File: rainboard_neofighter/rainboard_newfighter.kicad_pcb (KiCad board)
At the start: 2 copper layers, 270.2 x 259 mm, 95 parts, among them J1 Conn_01x02, J10 Conn_01x03, J11 SDS-50J, J12 SDS-50J, J13 Conn_01x02, J14 Conn_01x02, J15 Conn_01x02, J16 Conn_01x02, J17 Conn_01x02, J18 Conn_01x02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

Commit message: use corrent JST-HX connector
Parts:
- J1, J13, J14, J15, J16, J17, J18, J2, J3, J4, J5, J6, J7, J8: footprint Connector_JST:JST_XH_S2B-XH-A-1_1x02_P2.50mm_Horizontal -> Connector_JST:JST_XH_B2B-XH-AM_1x02_P2.50mm_Vertical
- J10, J9: footprint Connector_JST:JST_XH_S3B-XH-A-1_1x03_P2.50mm_Horizontal -> Connector_JST:JST_XH_B3B-XH-A_1x03_P2.50mm_Vertical
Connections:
- XA1 pad D17: Net-(XA1-PadD17) -> button-38
- XA1 pad D18: button-28 -> MIDI-OUT
- XA1 pad D19: button-38 -> MIDI-IN
- XA1 pad D21: Net-(XA1-PadD21) -> button-28

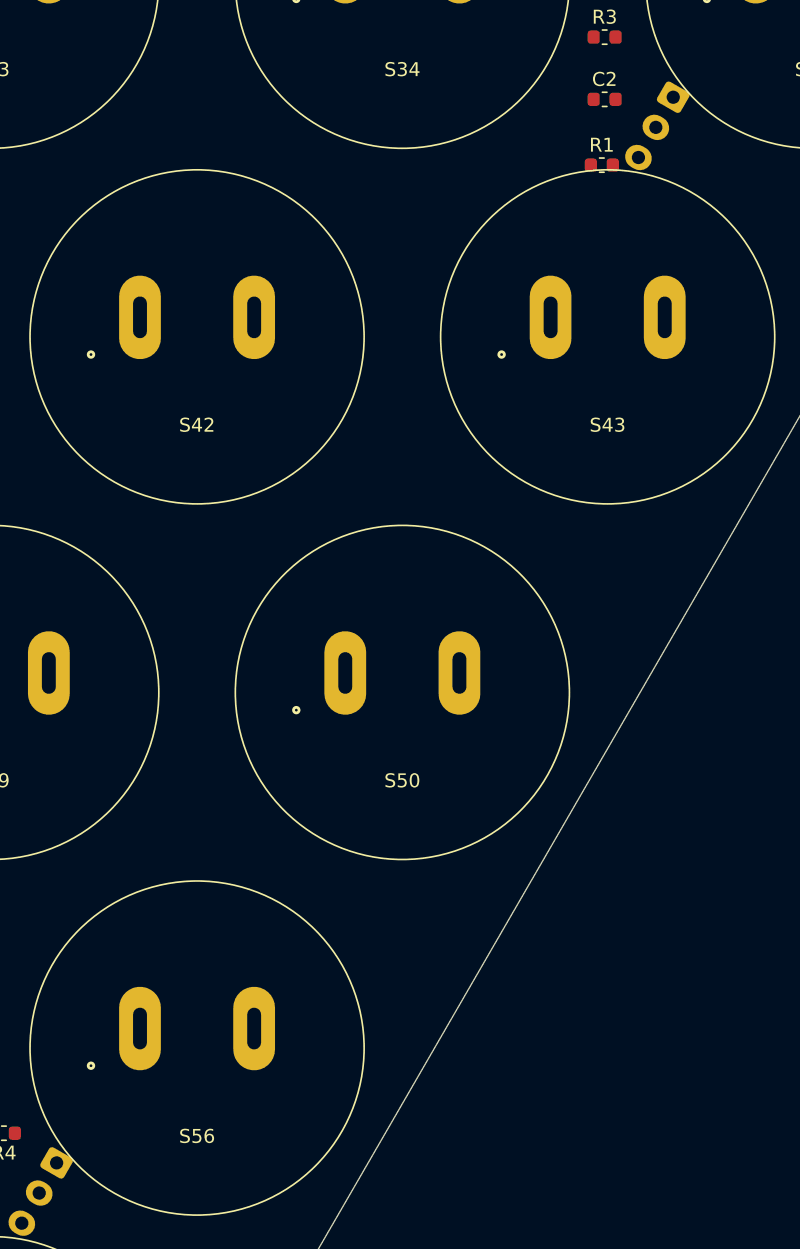
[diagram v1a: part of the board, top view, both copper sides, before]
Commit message: use corrent JST-HX connector
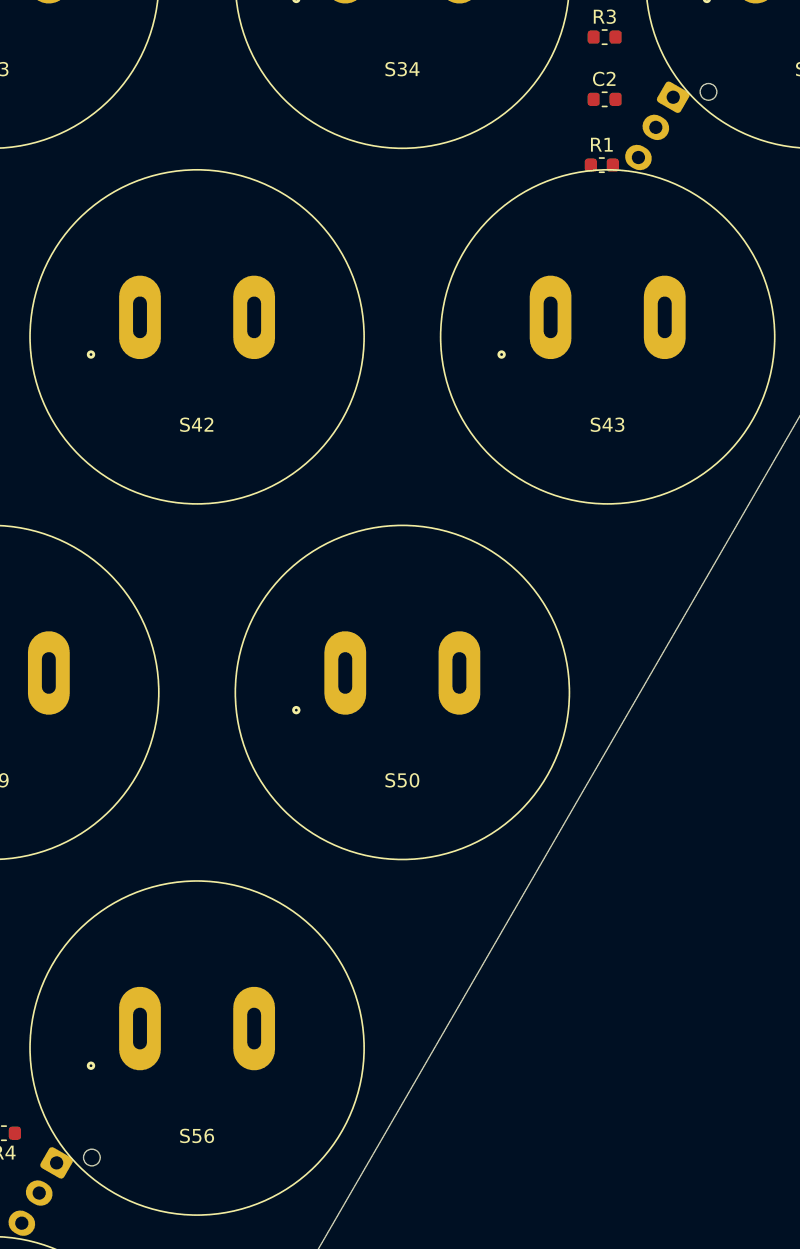
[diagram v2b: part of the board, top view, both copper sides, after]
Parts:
- J10, J9: footprint Connector_JST:JST_XH_B3B-XH-A_1x03_P2.50mm_Vertical -> Connector_JST:JST_XH_B3B-XH-AM_1x03_P2.50mm_Vertical

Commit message: final board outline dimentions
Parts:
- moved C1 39.1 mm to (0.41, -77.1)
- moved J11 8.70 mm to (-36.0, 128.2)
- moved J12 7.83 mm to (-15.3, 128.1)
- moved R1 6.67 mm to (96.2, 12.8)
- moved R4 3.75 mm to (59.3, 79.0)
- moved R5 3.28 mm to (-51.4, 119.5)
- moved C2 2.84 mm to (100.2, 8.99)
- moved C4 2.60 mm to (-56.2, 120.5)
- moved XA1 2.35 mm to (43.5, 137.5)
- moved R2 2.14 mm to (54.8, 86.6)
- moved R6 0.65 mm to (-43.7, 121.7)
- moved R3 0.37 mm to (102.7, 4.11)
- turned S39 to 0 degrees
- turned S41 to 0 degrees
- turned S59 to 270 degrees
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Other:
- board size 270.2 x 259 mm -> 260 x 253.6 mm

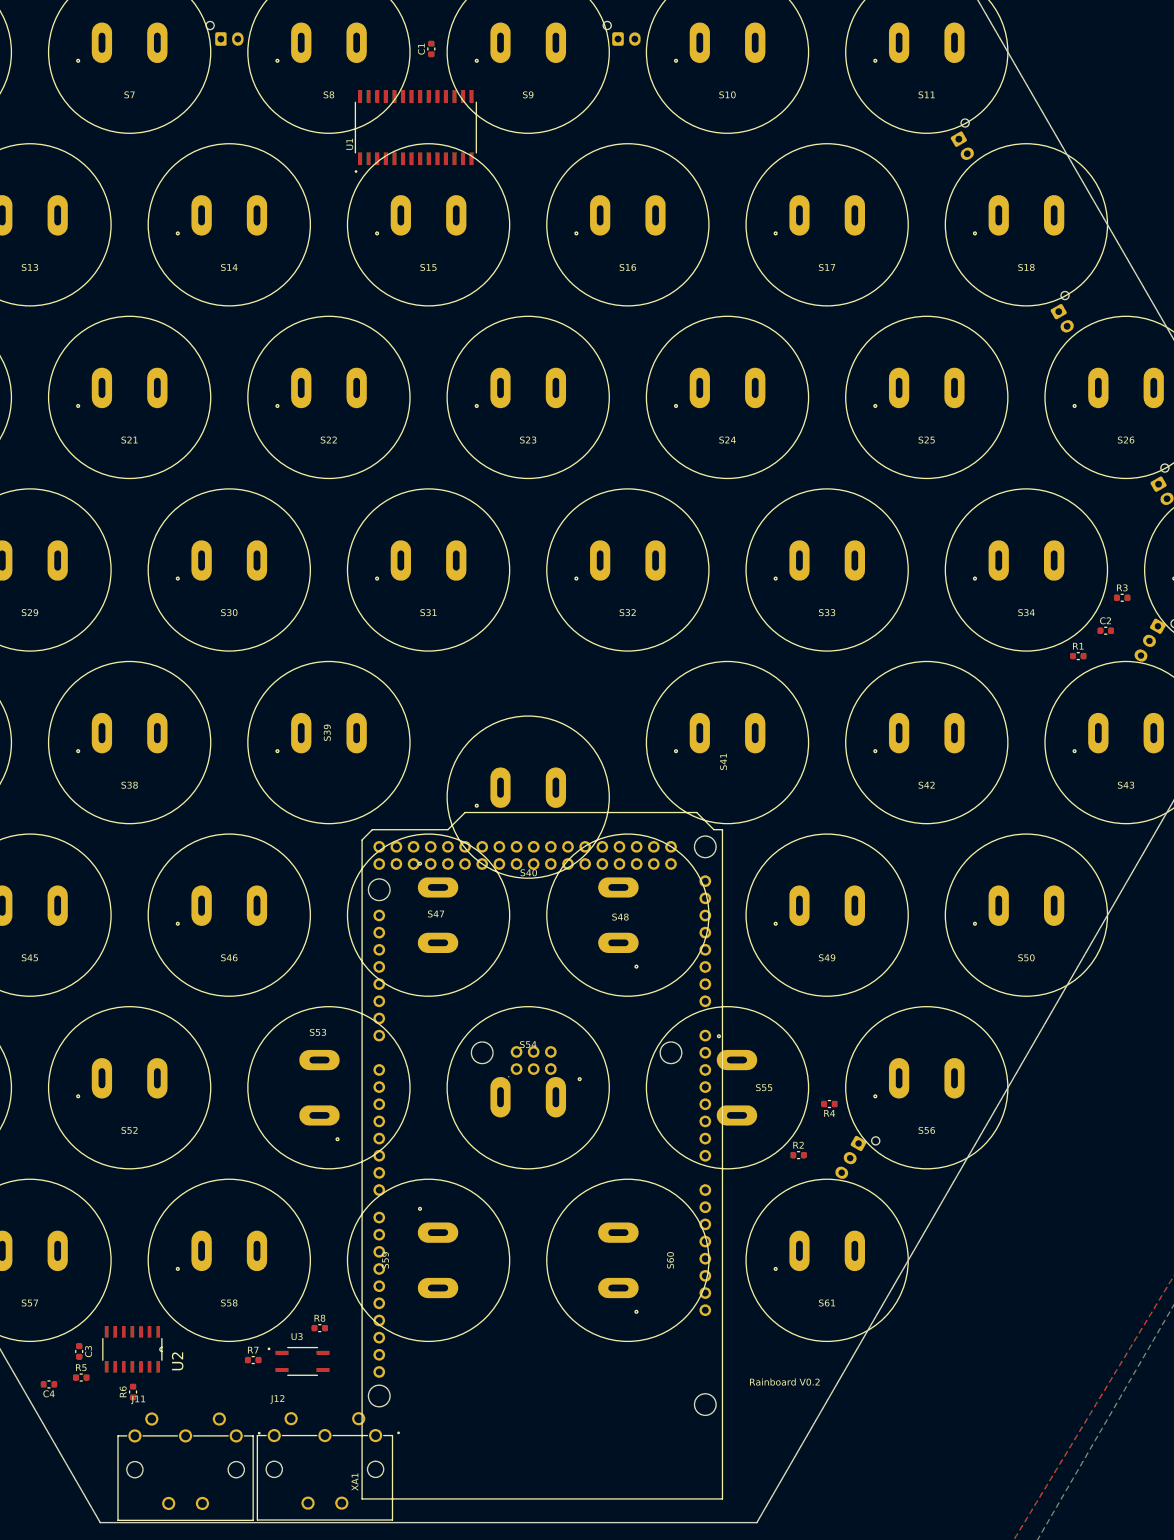
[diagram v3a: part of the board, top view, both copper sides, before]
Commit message: move decoupling caps close to ICs
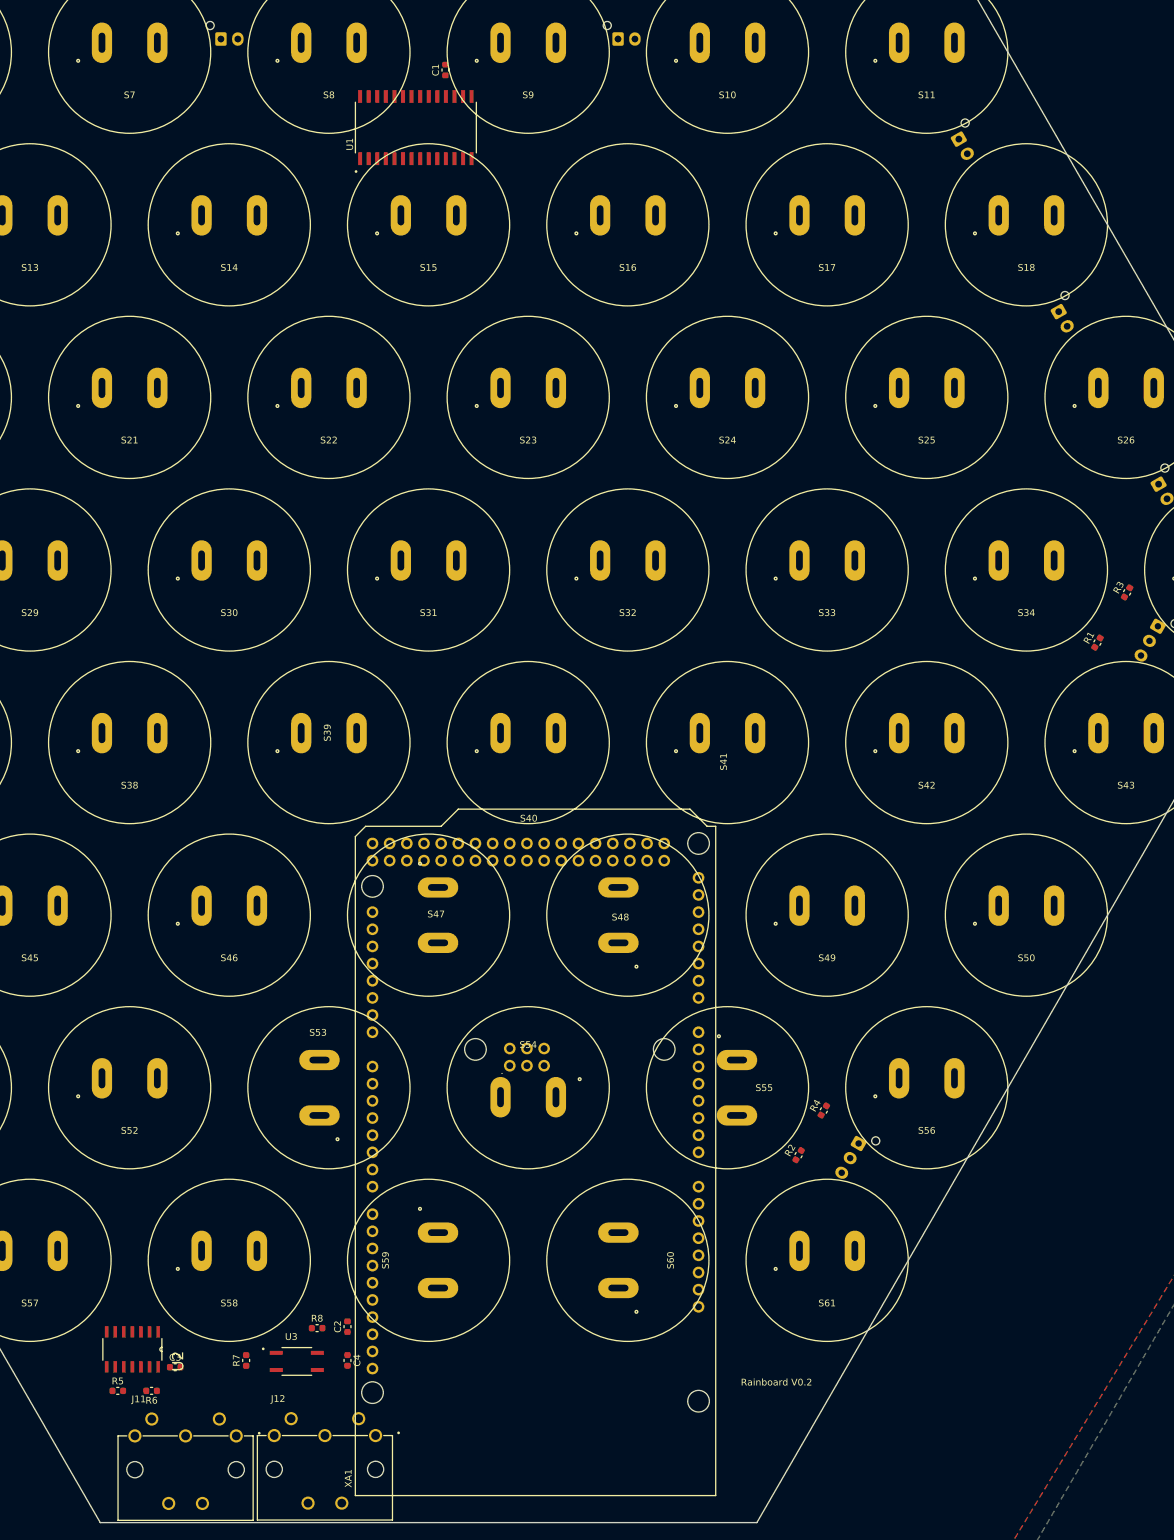
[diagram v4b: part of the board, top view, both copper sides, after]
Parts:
- moved C2 152.3 mm to (-12.0, 112.0), turned to 90 degrees
- moved C4 44.3 mm to (-12.0, 117.0), turned to 270 degrees
- moved C3 14.4 mm to (-37.5, 118.0), turned to 0 degrees
- moved S40 8.08 mm to (14.7, 25.5)
- moved R5 5.76 mm to (-46.0, 121.5)
- moved C1 3.75 mm to (2.50, -74.0)
- moved R1 3.47 mm to (99.0, 10.8), turned to 60 degrees
- moved R6 2.74 mm to (-41.0, 121.5), turned to 180 degrees
- moved R4 1.27 mm to (58.5, 80.0), turned to 60 degrees
- moved XA1 1.12 mm to (42.5, 137.0)
- moved R3 1.08 mm to (103.4, 3.32), turned to 60 degrees
- moved R7 1.04 mm to (-27.0, 117.0), turned to 90 degrees
- moved U3 0.86 mm to (-19.5, 117.1)
- moved R8 0.40 mm to (-16.5, 112.2)
- turned R2 to 60 degrees

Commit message: Add LCSC JLCPCB part data for each component
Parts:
- C1, C2, C3, C4: value 0.1uf -> 100nf
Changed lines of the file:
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@@
       (effects (font (size 1 1) (thickness 0.15)))
     )
-    (fp_text value 0.1uf (at 0 1.43 90) (layer F.Fab)
+    (fp_text value 100nf (at 0 1.43 90) (layer F.Fab)
       (effects (font (size 1 1) (thickness 0.15)))
     )
@@
       (effects (font (size 1 1) (thickness 0.15)))
     )
-    (fp_text value 0.1uf (at 0 1.43) (layer F.Fab)
+    (fp_text value 100nf (at 0 1.43) (layer F.Fab)
       (effects (font (size 1 1) (thickness 0.15)))
     )
@@
       (effects (font (size 1 1) (thickness 0.15)))
     )
-    (fp_text value 0.1uf (at 0 1.43 90) (layer F.Fab)
+    (fp_text value 100nf (at 0 1.43 90) (layer F.Fab)
       (effects (font (size 1 1) (thickness 0.15)))
     )
@@
       (effects (font (size 1 1) (thickness 0.15)))
     )
-    (fp_text value 0.1uf (at 0 1.43 90) (layer F.Fab)
-      (effects (font (size 1 1) (thickness 0.15)))
-    )
+    (fp_text value 100nf (at 0 1.43 90) (layer F.Fab)
+      (effects (font (size 1 1) (thickness 0.15)))
+    )

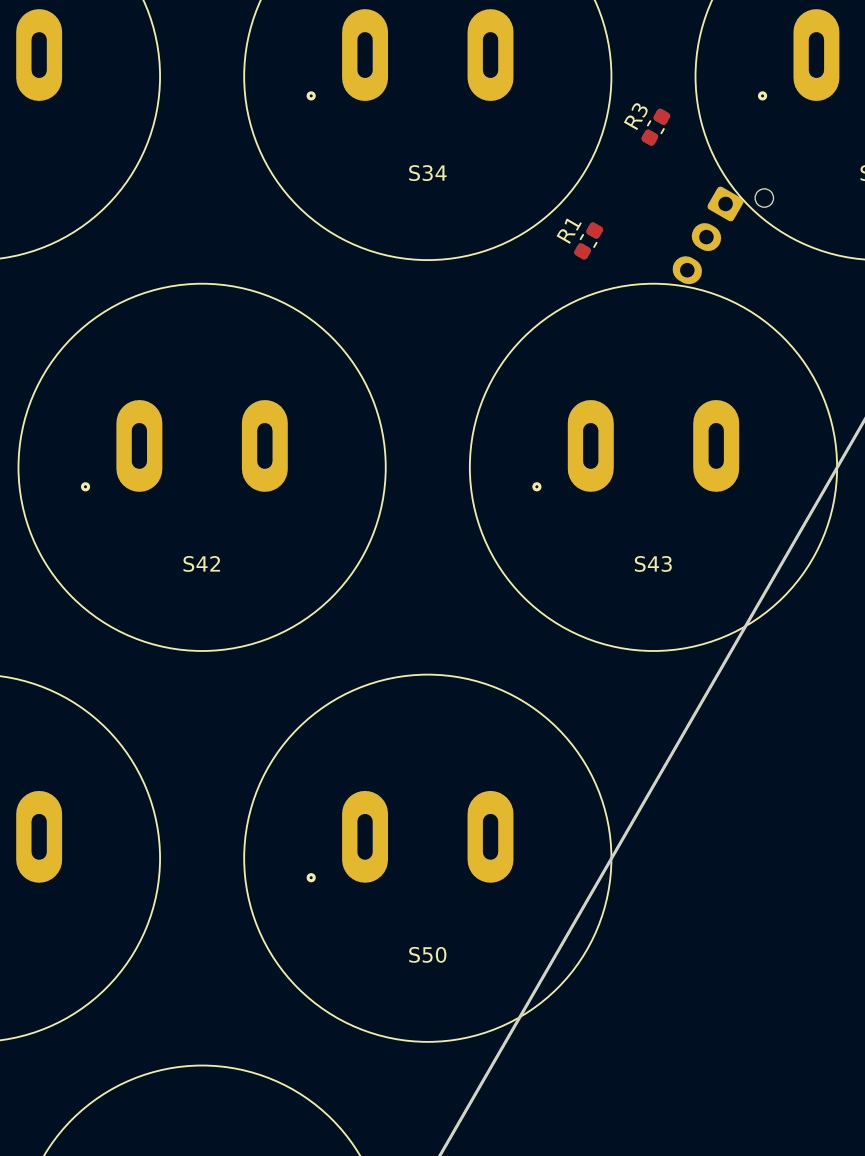
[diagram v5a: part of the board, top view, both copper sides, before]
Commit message: Move softpot headers to same corner
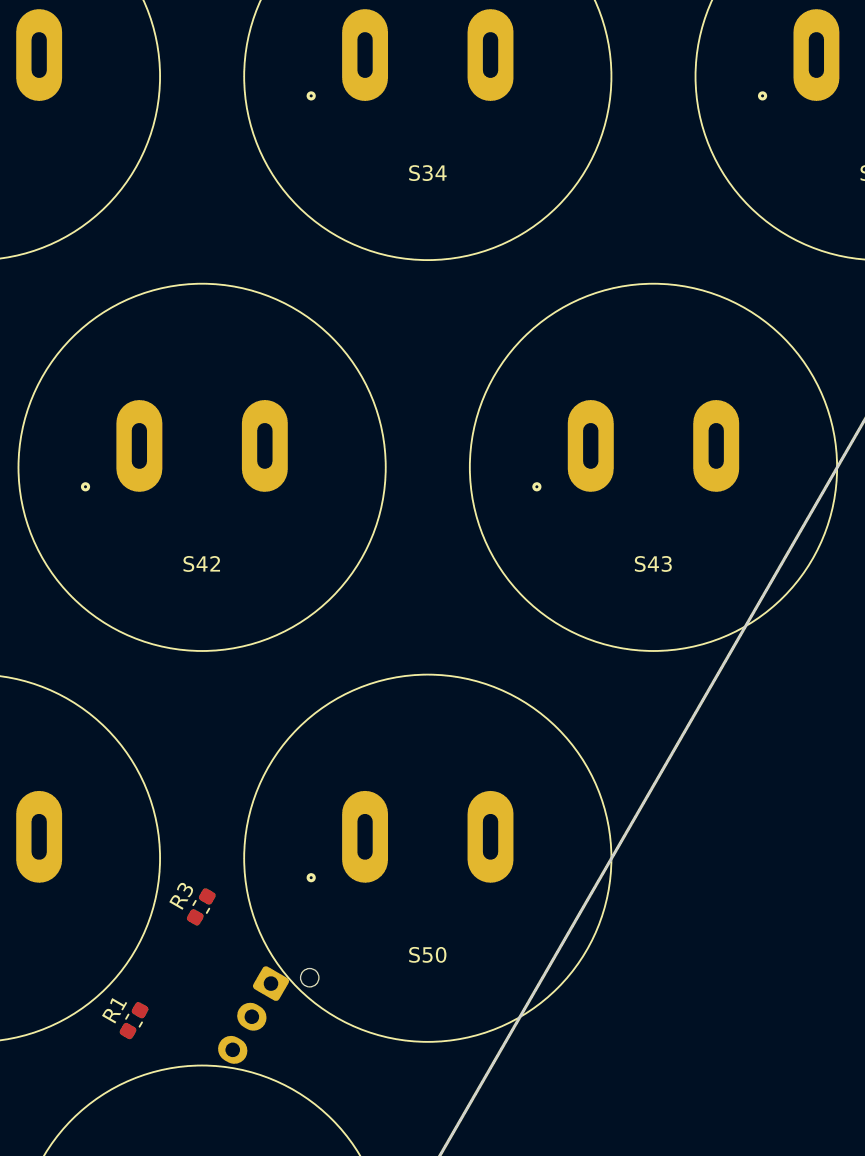
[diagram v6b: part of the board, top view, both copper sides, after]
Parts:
- moved R1 59.0 mm to (69.3, 61.7)
- moved J9 59.0 mm to (78.2, 59.3)
- moved R3 59.0 mm to (73.7, 54.3)
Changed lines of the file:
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@@
   )
   (module Connector_JST:JST_XH_B3B-XH-AM_1x03_P2.50mm_Vertical (layer B.Cu)
-    (at 107.95 8.3312 240)
+    (at 78.243583 59.281554 240)
     (descr "JST XH series connector, B3B-XH-AM, with boss (http://www.jst-mfg.com/product/pdf/eng/eXH.pdf), generated with kicad-footprint-generator")
     (tags "connector JST XH vertical boss")
@@
   )
   (module Resistor_SMD:R_0603_1608Metric (layer F.Cu)
-    (at 103.39375 3.318005 60)
+    (at 73.687333 54.268359 60)
     (descr "Resistor SMD 0603 (1608 Metric), square (rectangular) end terminal, IPC_7351 nominal, (Body size source: http://www.tortai-tech.com/upload/download/2011102023233369053.pdf), generated with kicad-footprint-generator")
     (tags resistor)
@@
   )
   (module Resistor_SMD:R_0603_1608Metric (layer F.Cu)
-    (at 99 10.7508 60)
+    (at 69.293583 61.701154 60)
     (descr "Resistor SMD 0603 (1608 Metric), square (rectangular) end terminal, IPC_7351 nominal, (Body size source: http://www.tortai-tech.com/upload/download/2011102023233369053.pdf), generated with kicad-footprint-generator")
     (tags resistor)
